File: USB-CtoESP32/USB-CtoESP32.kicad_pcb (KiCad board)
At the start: 2 copper layers, 24 parts, among them J1 USB_C_Receptacle_USB2.0_14P, J2 Conn_01x04_Pin, U1 LM1117MP-3.3, U2 CH340G, Y1 12MHz

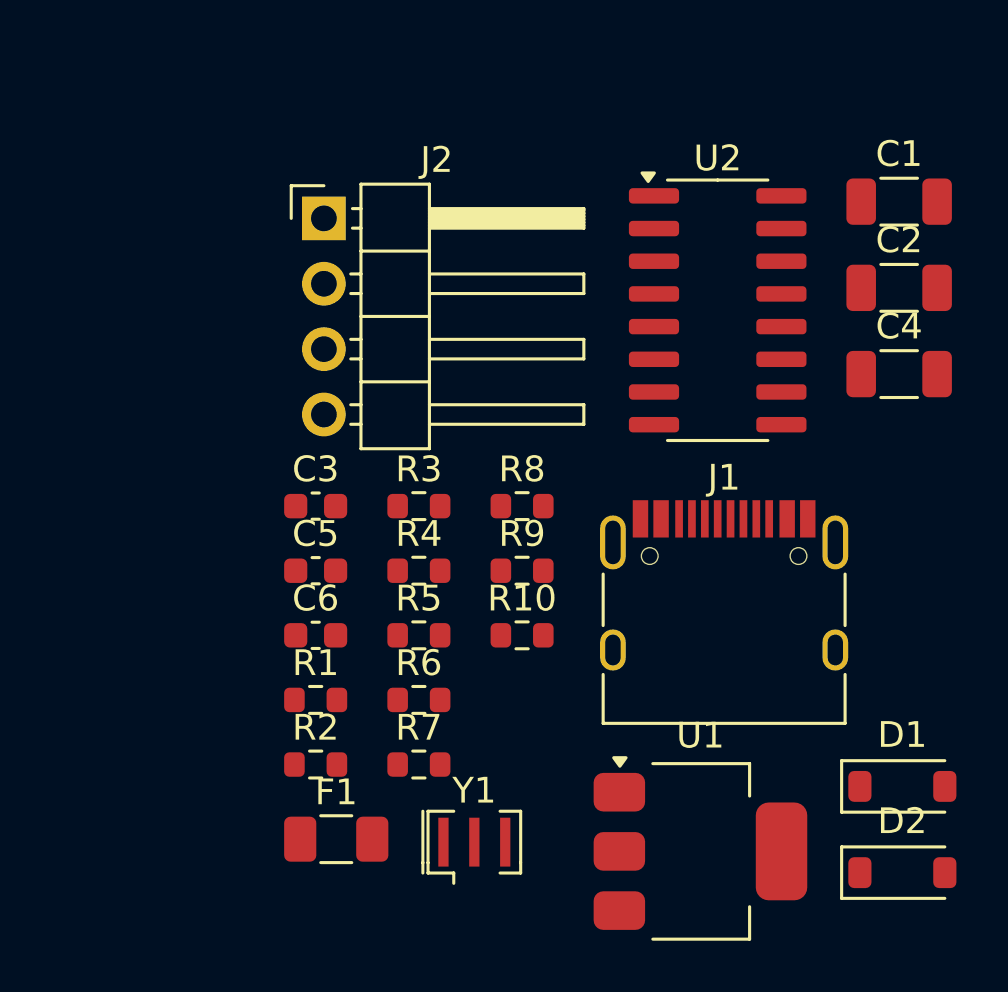
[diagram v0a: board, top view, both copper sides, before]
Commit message: Add files via upload
ENとIO0を追加
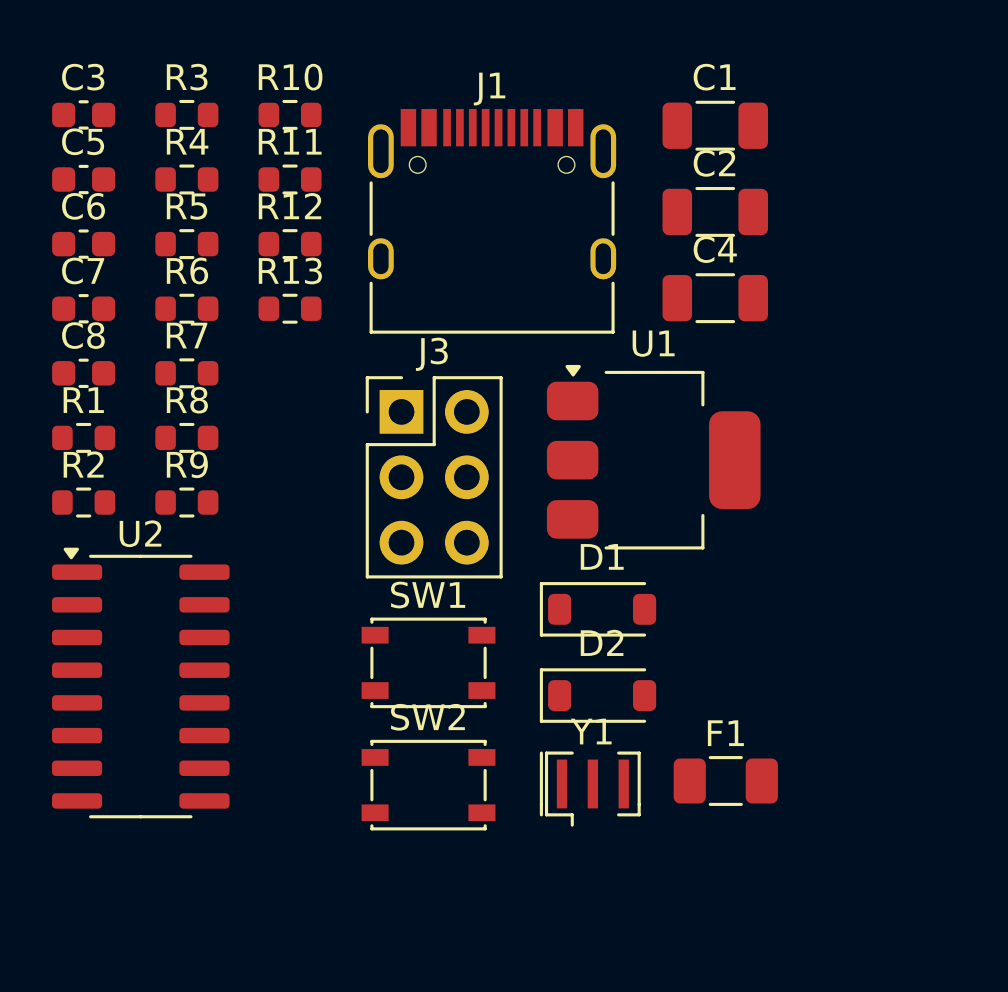
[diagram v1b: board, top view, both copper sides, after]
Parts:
- removed J2: Conn_01x04_Pin, Connector_PinHeader_2.54mm:PinHeader_1x04_P2.54mm_Horizontal
- added C7: 0.47u, Capacitor_SMD:C_0603_1608Metric, F.Cu at (28.1, 36.1)
- added C8: 1000p, Capacitor_SMD:C_0603_1608Metric, F.Cu at (28.1, 38.6)
- added J3: ICSP, Connector_PinHeader_2.54mm:PinHeader_2x03_P2.54mm_Vertical, F.Cu at (40.5, 40.1)
- added R11: 10k, Resistor_SMD:R_0603_1608Metric, F.Cu at (36.1, 31.1)
- added R12: 100, Resistor_SMD:R_0603_1608Metric, F.Cu at (36.1, 33.6)
- added R13: 10k, Resistor_SMD:R_0603_1608Metric, F.Cu at (36.1, 36.1)
- added SW1: RST, Button_Switch_SMD:SW_SPST_PTS810, F.Cu at (41.5, 49.8)
- added SW2: BOOT, Button_Switch_SMD:SW_SPST_PTS810, F.Cu at (41.5, 54.6)
- moved U2 26.8 mm to (30.3, 50.8)
- moved R10 22.1 mm to (36.1, 28.6)
- moved C6 17.7 mm to (28.1, 33.6)
- moved R5 17.7 mm to (32.1, 33.6)
- moved R6 17.7 mm to (32.1, 36.1)
- moved R3 17.7 mm to (32.1, 28.6)
- moved R4 17.7 mm to (32.1, 31.1)
- moved C3 17.7 mm to (28.1, 28.6)
- moved C5 17.7 mm to (28.1, 31.1)
- moved J1 17.7 mm to (44.0, 33.1)
- moved R7 17.7 mm to (32.1, 38.6)
- moved U1 15.3 mm to (50.3, 42.0)
- moved F1 15.3 mm to (53.1, 54.4)
- moved R1 13.6 mm to (28.1, 41.1)
- moved R2 13.6 mm to (28.1, 43.6)
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
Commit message: Add files via upload
配線終了。
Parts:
- C1: footprint Capacitor_SMD:C_1206_3216Metric -> Capacitor_SMD:C_0603_1608Metric; moved to B.Cu
- C2, C4: footprint Capacitor_SMD:C_1206_3216Metric -> Capacitor_SMD:C_0603_1608Metric
- C3, C5, C6, C7, C8, D1, D2, R1, R10, R11, R12, R13, R2, R3, R4, R5, R8, R9, U2, Y1: moved to B.Cu
- J3: footprint Connector_PinHeader_2.54mm:PinHeader_2x03_P2.54mm_Vertical -> Connector_PinHeader_2.54mm:PinHeader_2x03_P2.54mm_Horizontal
- moved C7 65.0 mm to (80.6, 74.5), turned to 180 degrees
- moved R11 63.2 mm to (80.6, 76.0), turned to 180 degrees
- moved R10 62.8 mm to (80.6, 73.0), turned to 180 degrees
- moved C8 60.3 mm to (80.6, 68.4)
- moved C3 57.6 mm to (65.4, 72.5), turned to 90 degrees
- moved R12 57.4 mm to (80.6, 69.9), turned to 180 degrees
- moved R8 57.1 mm to (80.6, 71.4), turned to 180 degrees
- moved C5 56.4 mm to (71.2, 67.5), turned to 90 degrees
- moved R4 54.6 mm to (72.8, 67.5), turned to -90 degrees
- moved R5 54.4 mm to (74.7, 67.5), turned to -90 degrees
- moved R9 53.7 mm to (80.6, 66.8), turned to 180 degrees
- moved R3 52.6 mm to (62.7, 71.4), turned to 180 degrees
- moved R6 51.6 mm to (69.7, 71.5), turned to -90 degrees
- moved J3 51.5 mm to (83.2, 68.9)
- moved C6 50.1 mm to (63.5, 69.1), turned to 90 degrees
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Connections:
- C3 pad 1: Net-(D1-K) -> GND
- C3 pad 2: Net-(U2-VCC) -> Net-(D1-K)
- U2 pad 16: Net-(U2-VCC) -> Net-(D1-K)
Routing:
- net GND: track 0.00 -> 42.5 mm, vias 0 -> 13
- net +3V3: track 0.00 -> 31.4 mm, vias 0 -> 1
- net Net-(C8-Pad1): track 0.00 -> 23.8 mm, vias 0 -> 2
- net Net-(J1-SHIELD): track 0.00 -> 18.8 mm
- net Net-(U2-RXD): track 0.00 -> 18.6 mm
- net Net-(J1-D+-PadA6): track 0.00 -> 18.2 mm, vias 0 -> 1
- net Net-(F1-Pad2): track 0.00 -> 18.1 mm
- net Net-(D1-K): track 0.00 -> 16.7 mm, vias 0 -> 1
- net Net-(U2-TXD): track 0.00 -> 14.2 mm
- net Net-(J1-D--PadA7): track 0.00 -> 13.9 mm, vias 0 -> 1
- net EN: track 0.00 -> 13.3 mm, vias 0 -> 1
- net Net-(D1-A): track 0.00 -> 8.15 mm, vias 0 -> 1
- net Net-(J1-CC2): track 0.00 -> 5.60 mm, vias 0 -> 1
- net Net-(U2-UD+): track 0.00 -> 5.48 mm
- net TX: track 0.00 -> 5.15 mm
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- added copper zone on B.Cu, net GND
- added copper zone on F.Cu, net GND
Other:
- board outline added: 32.3 x 11.4 mm

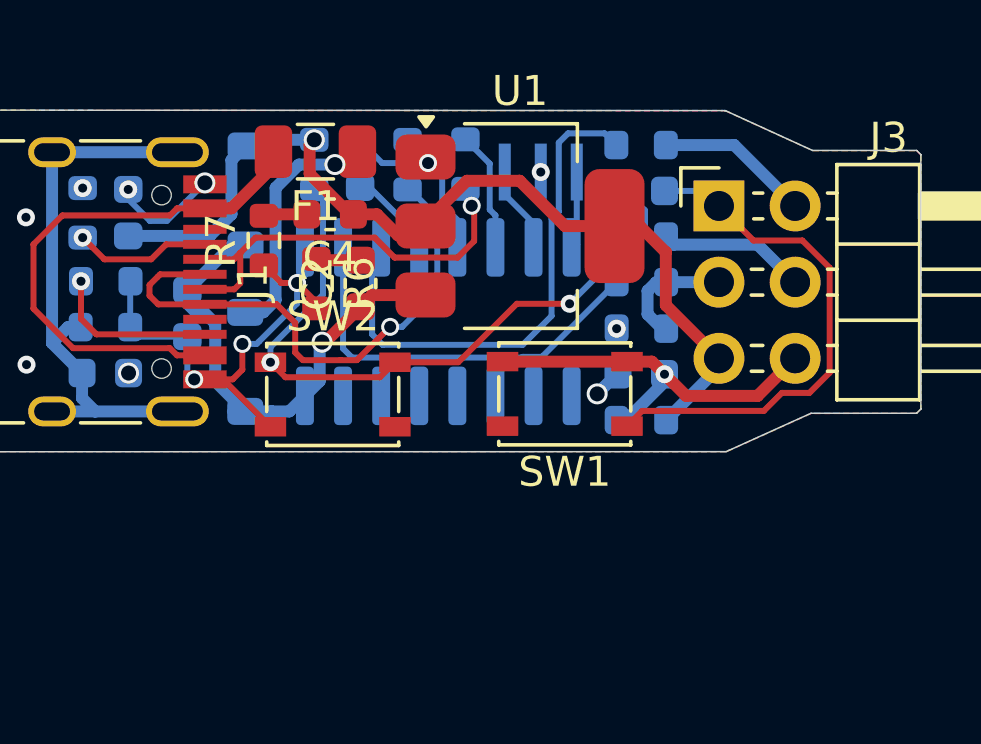
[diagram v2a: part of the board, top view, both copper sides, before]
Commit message: Add files via upload
入江さんからのフィードバックを回路図に反映
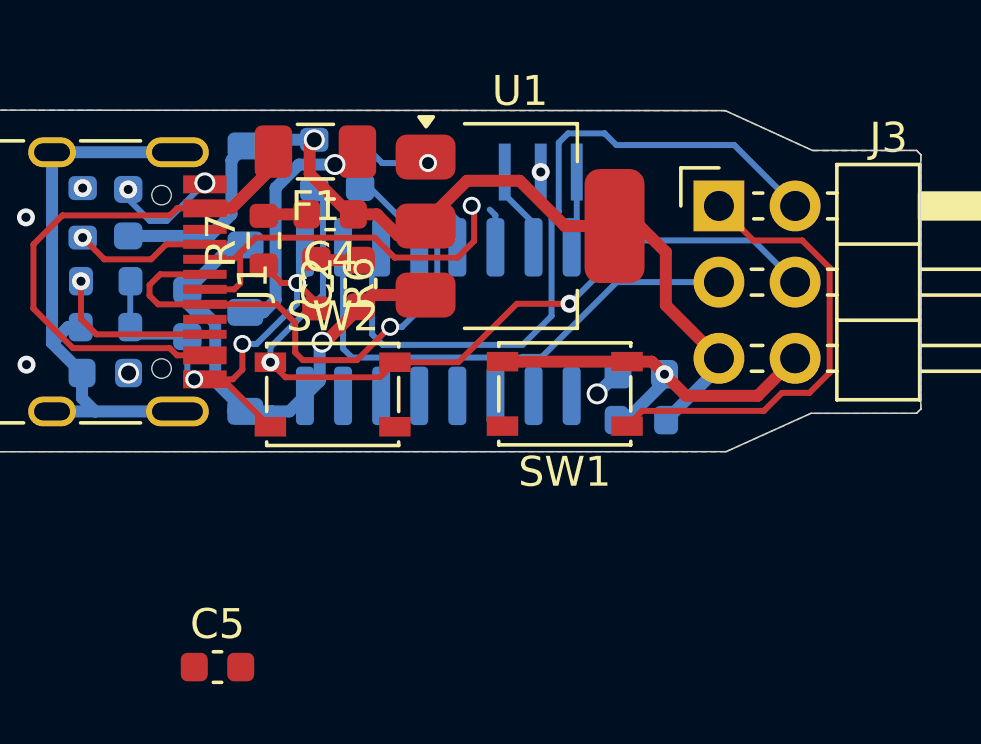
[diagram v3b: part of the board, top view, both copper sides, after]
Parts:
- removed C8: 1000p, Capacitor_SMD:C_0603_1608Metric
- removed R10: 6.8k, Resistor_SMD:R_0603_1608Metric
- removed R12, R9: 100, Resistor_SMD:R_0603_1608Metric
- removed R4, R5: 22, Resistor_SMD:R_0603_1608Metric
- removed R8: 3.3k, Resistor_SMD:R_0603_1608Metric
- added C5: 0.1u, Capacitor_SMD:C_0603_1608Metric, F.Cu at (66.4, 84.2)
- C7: value 0.47u -> 1u
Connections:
- C3 pad 2: Net-(D1-K) -> +3V3
- J1 pad A6: Net-(J1-D+-PadA6) -> Net-(U2-UD+)
- J1 pad A7: Net-(J1-D--PadA7) -> Net-(U2-UD-)
- J1 pad B6: Net-(J1-D+-PadA6) -> Net-(U2-UD+)
- J1 pad B7: Net-(J1-D--PadA7) -> Net-(U2-UD-)
- R13 pad 2: Net-(C8-Pad1) -> IO0
- SW2 pad 1: Net-(C8-Pad1) -> IO0
- U2 pad 16: Net-(D1-K) -> +3V3
- U2 pad 2: Net-(U2-TXD) -> RX
- U2 pad 3: Net-(U2-RXD) -> TX
- U2 pad 4: Net-(U2-V3) -> +3V3
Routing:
- net Net-(C8-Pad1): track 23.8 -> 0.00 mm, vias 2 -> 0
- net IO0: track 4.93 -> 27.2 mm, vias 0 -> 2
- net TX: track 5.15 -> 25.4 mm
- net Net-(U2-RXD): track 18.6 -> 0.00 mm
- net Net-(J1-D+-PadA6): track 18.2 -> 0.00 mm, vias 1 -> 0
- net Net-(U2-TXD): track 14.2 -> 0.00 mm
- net Net-(J1-D--PadA7): track 13.9 -> 0.00 mm, vias 1 -> 0
- net Net-(U2-UD+): track 5.48 -> 19.0 mm, vias 0 -> 1
- net RX: track 4.11 -> 17.6 mm
- net Net-(U2-UD-): track 4.01 -> 14.6 mm, vias 0 -> 1
- net GND: track 42.5 -> 41.2 mm, vias 13 -> 12

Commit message: Add files via upload
入江さん承認済み。未配線
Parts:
- removed the C5 at (66.4, 84.2)
- removed the C5 at (71.2, 67.5)
- added C5: 0.1u, Capacitor_SMD:C_0603_1608Metric, F.Cu at (36.9, 62.4)
- C1, C3, C6, C7, D1, D2, R1, R11, R13, R2, R3, U2, Y1: moved to F.Cu
- moved J3 52.4 mm to (37.2, 43.7)
- moved C7 44.3 mm to (40.9, 54.9), turned to 0 degrees
- moved R11 40.2 mm to (44.9, 57.4), turned to 0 degrees
- moved C2 38.1 mm to (36.9, 54.9), turned to 0 degrees
- moved U1 36.8 mm to (39.8, 67.9)
- moved C4 34.6 mm to (36.9, 59.9), turned to 0 degrees
- moved C1 34.0 mm to (36.9, 52.4)
- moved D1 33.8 mm to (53.7, 43.1), turned to 0 degrees
- moved C3 32.3 mm to (36.9, 57.4), turned to 0 degrees
- moved R6 31.3 mm to (44.9, 52.4), turned to 0 degrees
- moved C6 28.1 mm to (40.9, 52.4), turned to 0 degrees
- moved Y1 27.9 mm to (59.1, 46.5)
- moved R7 27.6 mm to (44.9, 54.9), turned to 0 degrees
- moved R1 26.8 mm to (40.9, 57.4)
- moved F1 26.1 mm to (59.4, 43.1), turned to 0 degrees
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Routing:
- net GND: track 41.2 -> 0.00 mm, vias 12 -> 0
- net +3V3: track 31.4 -> 0.00 mm, vias 1 -> 0
- net IO0: track 27.2 -> 0.00 mm, vias 2 -> 0
- net TX: track 25.4 -> 0.00 mm
- net Net-(U2-UD+): track 19.0 -> 0.00 mm, vias 1 -> 0
- net Net-(J1-SHIELD): track 18.8 -> 0.00 mm
- net Net-(F1-Pad2): track 18.1 -> 0.00 mm
- net RX: track 17.6 -> 0.00 mm
- net Net-(D1-K): track 16.5 -> 0.00 mm, vias 1 -> 0
- net Net-(U2-UD-): track 14.6 -> 0.00 mm, vias 1 -> 0
- net EN: track 13.3 -> 0.00 mm, vias 1 -> 0
- net Net-(D1-A): track 8.15 -> 0.00 mm, vias 1 -> 0
- net Net-(J1-CC2): track 5.60 -> 0.00 mm, vias 1 -> 0
- net Net-(J1-CC1): track 4.58 -> 0.00 mm, vias 1 -> 0
- net Net-(U2-V3): track 3.86 -> 0.00 mm
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- removed copper zone on B.Cu, net GND
- removed copper zone on F.Cu, net GND
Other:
- board outline removed

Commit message: Add files via upload
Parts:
- moved J3 65.0 mm to (101.1, 55.7)
- moved C7 64.4 mm to (105.2, 51.7), turned to -90 degrees
- moved C2 60.7 mm to (97.5, 57.6)
- moved C1 60.4 mm to (96.8, 60.0), turned to 90 degrees
- moved R1 56.8 mm to (97.5, 62.2)
- moved C4 54.5 mm to (90.8, 51.7), turned to 90 degrees
- moved R6 54.1 mm to (98.5, 59.9), turned to -90 degrees
- moved C5 53.5 mm to (89.3, 51.7), turned to 90 degrees
- moved R11 53.3 mm to (98.2, 55.3), turned to 90 degrees
- moved C6 52.5 mm to (93.3, 54.9)
- moved U1 52.5 mm to (91.5, 59.3)
- moved R13 52.0 mm to (96.7, 55.4), turned to 90 degrees
- moved C3 51.2 mm to (87.8, 51.7), turned to 90 degrees
- moved R7 47.5 mm to (92.3, 51.6), turned to 90 degrees
- moved SW1 44.5 mm to (101.6, 52.0), turned to 180 degrees
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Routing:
- net GND: track 0.00 -> 91.9 mm, vias 0 -> 4
- net Net-(J1-SHIELD): track 0.00 -> 42.7 mm
- net +3V3: track 0.00 -> 38.5 mm
- net RX: track 0.00 -> 38.2 mm
- net TX: track 0.00 -> 32.8 mm
- net Net-(D1-K): track 0.00 -> 26.7 mm
- net EN: track 0.00 -> 21.2 mm
- net Net-(F1-Pad2): track 0.00 -> 16.1 mm
- net IO0: track 0.00 -> 14.0 mm, vias 0 -> 1
- net Net-(U2-UD-): track 0.00 -> 11.7 mm, vias 0 -> 3
- net Net-(U2-UD+): track 0.00 -> 10.9 mm
- net Net-(J1-CC2): track 0.00 -> 3.25 mm
- net Net-(J1-CC1): track 0.00 -> 3.18 mm
- net Net-(U2-XI): track 0.00 -> 2.90 mm
- net Net-(U2-XO): track 0.00 -> 2.57 mm
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- added copper zone on B.Cu, net GND
- added copper zone on F.Cu, net GND
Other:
- board outline added: 39.5 x 14.4 mm
